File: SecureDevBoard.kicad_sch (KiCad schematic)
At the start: 29 parts, among them J1 USB_C_Receptacle_USB2.0_14P, SW1 SW_Push, U1 RP2040, U2 NCP1117-3.3_SOT223, U3 W25Q128JVS, Y1 12 MHz

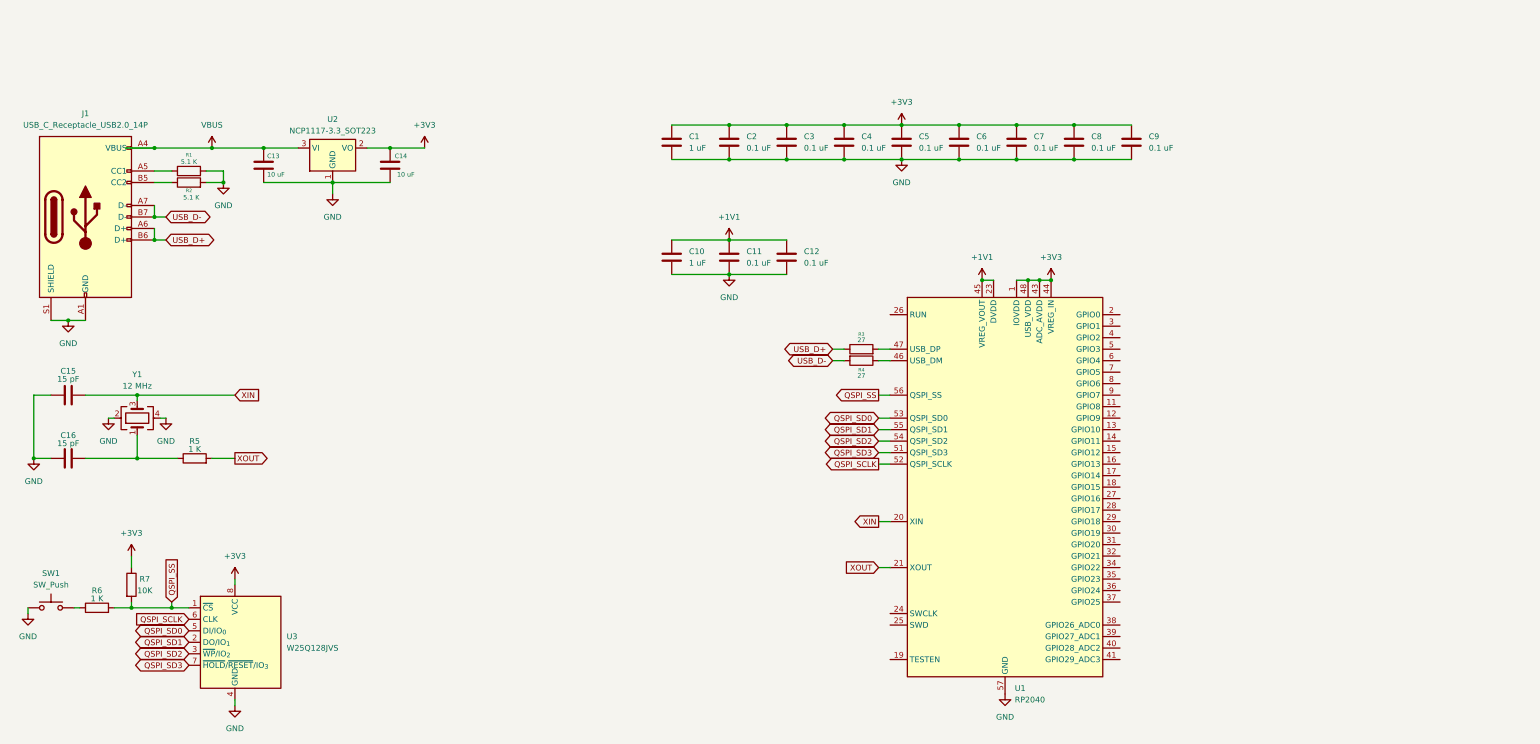
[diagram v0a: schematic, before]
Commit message: Journal2-Migrate RP2040 to RP2350b
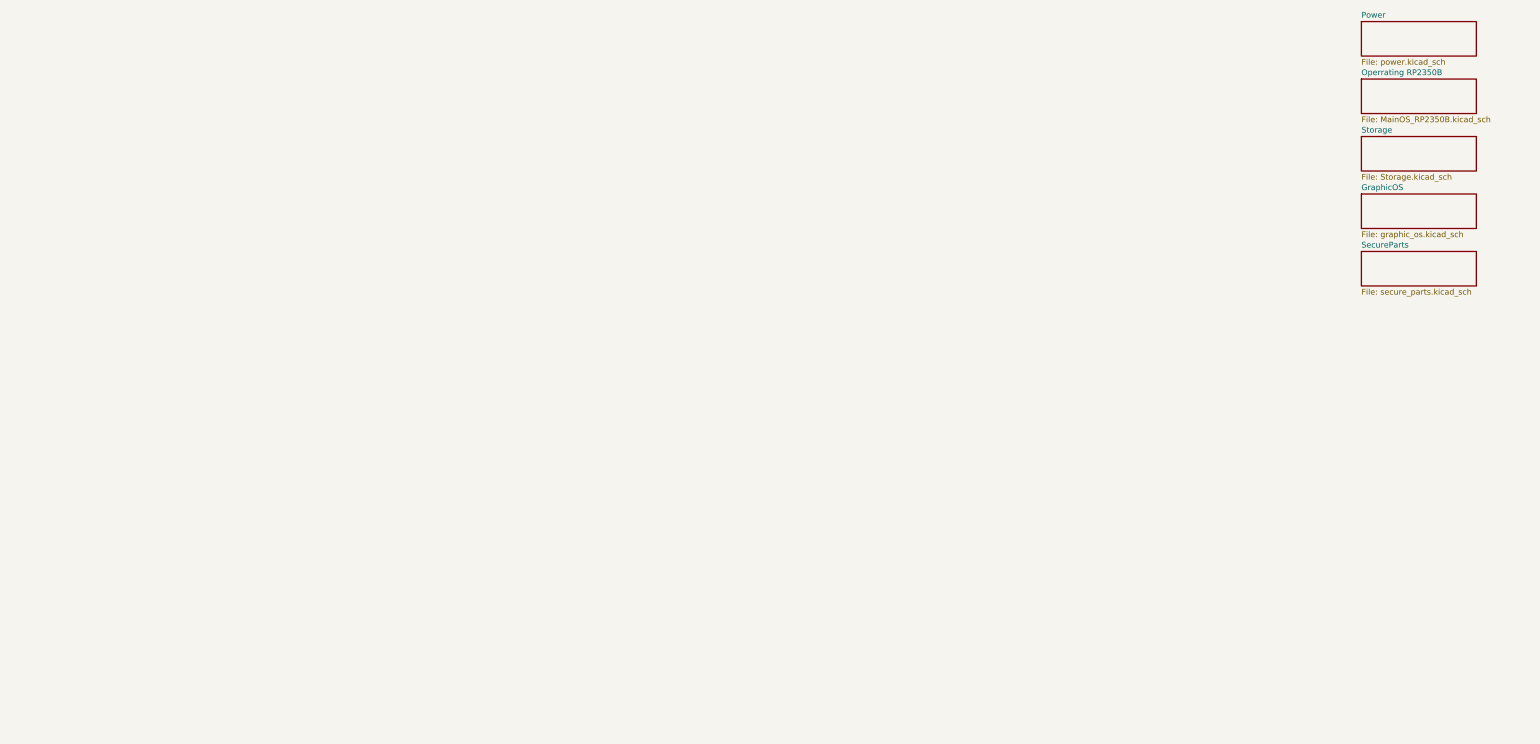
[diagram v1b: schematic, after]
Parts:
- removed C1, C10: 1 uF, symbol Device:C
- removed C11, C12, C2, C3, C4, C5, C6, C7, C8, C9: 0.1 uF, symbol Device:C
- removed C13, C14: 10 uF, symbol Device:C
- removed C15, C16: 15 pF, symbol Device:C
- removed J1: USB_C_Receptacle_USB2.0_14P, symbol Connector:USB_C_Receptacle_USB2.0_14P
- removed R1, R2: 5.1 K, symbol Device:R
- removed R3, R4: 27, symbol Device:R
- removed R5, R6: 1 K, symbol Device:R
- removed R7: 10K, symbol Device:R
- removed SW1: SW_Push, symbol Switch:SW_Push
- removed U1: RP2040, Package_DFN_QFN:QFN-56-1EP_7x7mm_P0.4mm_EP3.2x3.2mm, symbol MCU_RaspberryPi:RP2040
- removed U2: NCP1117-3.3_SOT223, Package_TO_SOT_SMD:SOT-223-3_TabPin2, symbol Regulator_Linear:NCP1117-3.3_SOT223
- removed U3: W25Q128JVS, Package_SO:SOIC-8_5.3x5.3mm_P1.27mm, symbol Memory_Flash:W25Q128JVS
- removed Y1: 12 MHz, symbol Device:Crystal_GND24
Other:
- added sheet GraphicOS (graphic_os.kicad_sch)
- added sheet Operrating RP2350B (MainOS_RP2350B.kicad_sch)
- added sheet Power (power.kicad_sch)
- added sheet SecureParts (secure_parts.kicad_sch)
- added sheet Storage (Storage.kicad_sch)

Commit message: Restore Local Backup
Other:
- added sheet Network (network.kicad_sch)
- added sheet PinHeaders (pin_headers.kicad_sch)
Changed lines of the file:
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@@
 	(paper "A4")
+	(sheet
+		(at 317.5 78.74)
+		(size 25.4 7.62)
+		(exclude_from_sim no)
+		(in_bom yes)
+		(on_board yes)
+		(dnp no)
+		(fields_autoplaced yes)
+		(stroke
+			(width 0.1524)
+			(type solid)
+		)
+		(fill
+			(color 0 0 0 0.0000)
+		)
+		(property "Sheetname" "PinHeaders"
+			(at 317.5 78.0284 0)
+			(effects
+				(font
+					(size 1.27 1.27)
+				)
+				(justify left bottom)
+			)
+		)
+		(property "Sheetfile" "pin_headers.kicad_sch"
+			(at 317.5 86.9446 0)
+			(effects
+				(font
+					(size 1.27 1.27)
+				)
+				(justify left top)
+			)
+		)
+		(instances
+			(project "SecureDevBoard"
+				(path "/c14388fe-d04a-4cf5-bac5-31c01c6a9ed5"
+					(page "8")
+				)
+			)
+		)
+	)
 	(sheet
 		(at 317.5 2.54)
@@
 				)
 			)
+		)
+	)
+	(sheet
+		(at 317.5 66.04)
+		(size 25.4 7.62)
+		(exclude_from_sim no)
+		(in_bom yes)
+		(on_board yes)
+		(dnp no)
+		(fields_autoplaced yes)
+		(stroke
+			(width 0.1524)
+			(type solid)
+		)
+		(fill
+			(color 0 0 0 0.0000)
+		)
+		(property "Sheetname" "Network"
+			(at 317.5 65.3284 0)
+			(effects
+				(font
+					(size 1.27 1.27)
+				)
+				(justify left bottom)
+			)
+		)
+		(property "Sheetfile" "network.kicad_sch"
+			(at 317.5 74.2446 0)
+			(effects
+				(font
+					(size 1.27 1.27)
+				)
+				(justify left top)
+			)
+		)
+		(instances
+			(project "SecureDevBoard"
+				(path "/c14388fe-d04a-4cf5-bac5-31c01c6a9ed5"
+					(page "7")
+				)
+			)
